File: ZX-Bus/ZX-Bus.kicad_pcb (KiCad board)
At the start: 2 copper layers, 177 x 146 mm, 51 parts, among them J1 DIP-40 Pins, J2 PLS-3, J3 PLS-6, J4 Power, J5 Main board power, J6 12V, J7 5V, J8 Reset, J9 PLS-2R, U1 Z84C00xxP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

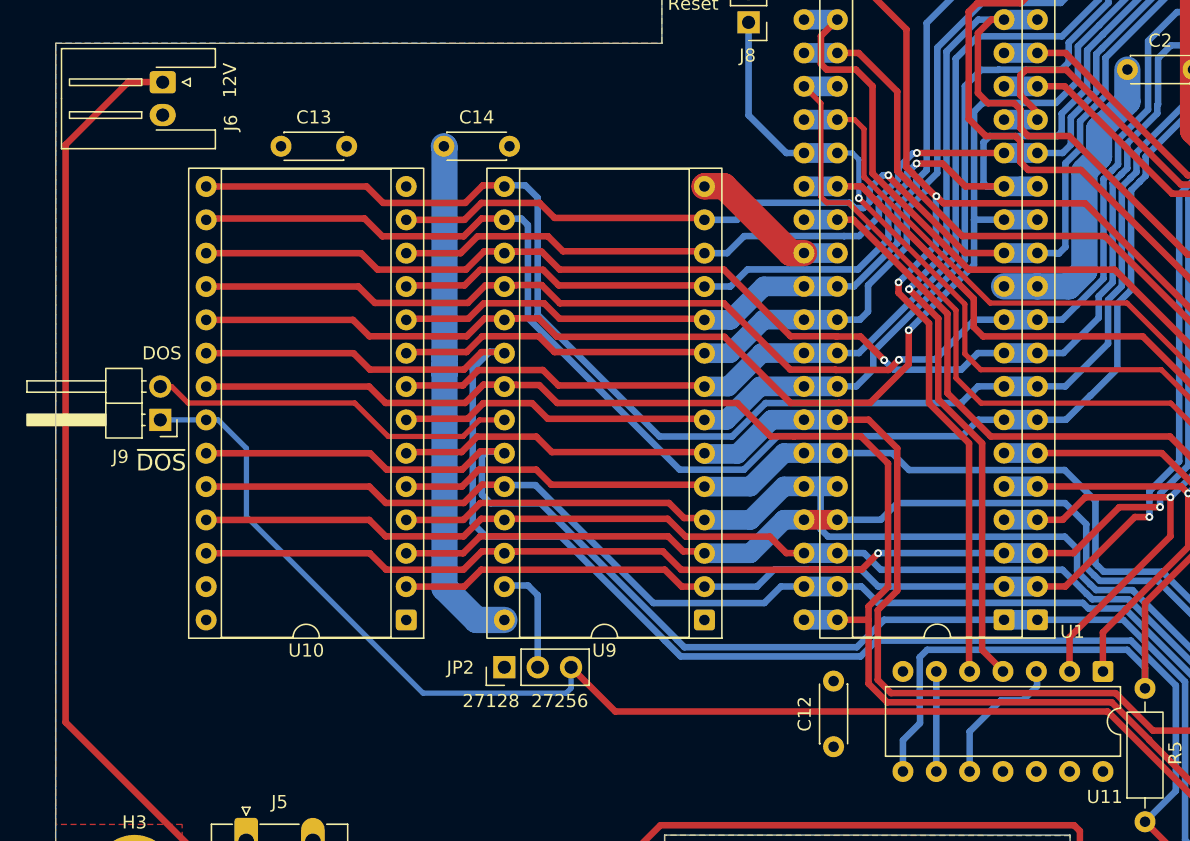
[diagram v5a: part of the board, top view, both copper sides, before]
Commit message: ZX-Bus: Fix ROM type select jumper
We actually need to switch two lines.
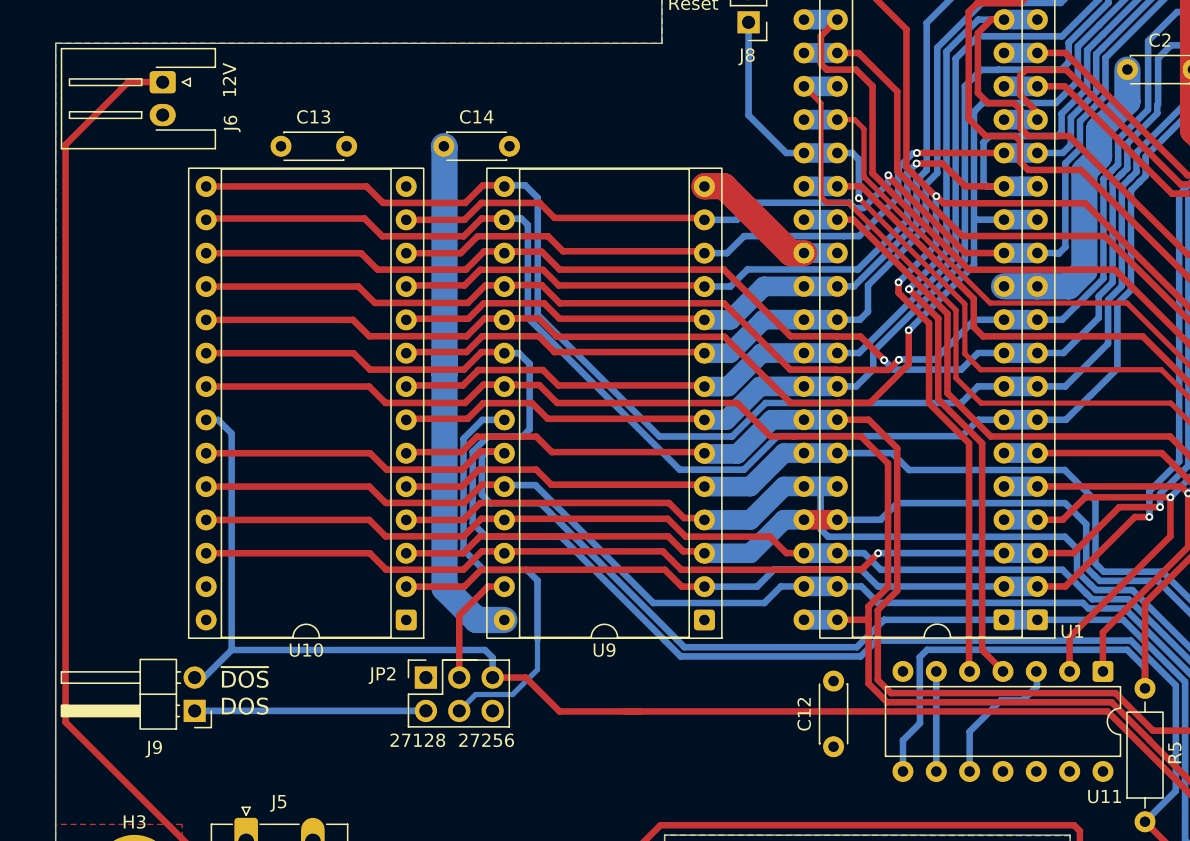
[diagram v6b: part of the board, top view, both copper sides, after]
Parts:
- JP2: footprint Connector_PinHeader_2.54mm:PinHeader_1x03_P2.54mm_Vertical -> Connector_PinHeader_2.54mm:PinHeader_3x09_P2.54mm_Vertical
- moved J9 22.3 mm to (26.4, 182.4)
- moved JP2 6.03 mm to (44.0, 179.8), turned to 0 degrees
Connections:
- J9 pad 1: /~{DOS} -> /DOS
- J9 pad 2: /DOS -> /~{DOS}
- U9 pad 22: /DOS -> Net-(U9-~{OE})
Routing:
- net Net-(U9-~{OE}): track 0.00 -> 32.8 mm
- net /DOS: track 28.3 -> 17.6 mm
- net /~{DOS}: track 258.5 -> 264.8 mm
- net /~{RDR}: track 327.3 -> 330.4 mm
- net Net-(U9-~{PGM}): track 8.33 -> 9.08 mm
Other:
- board text added: "~{DOS} DOS"
- board text removed: "DOS"
- board text removed: "~{DOS}"

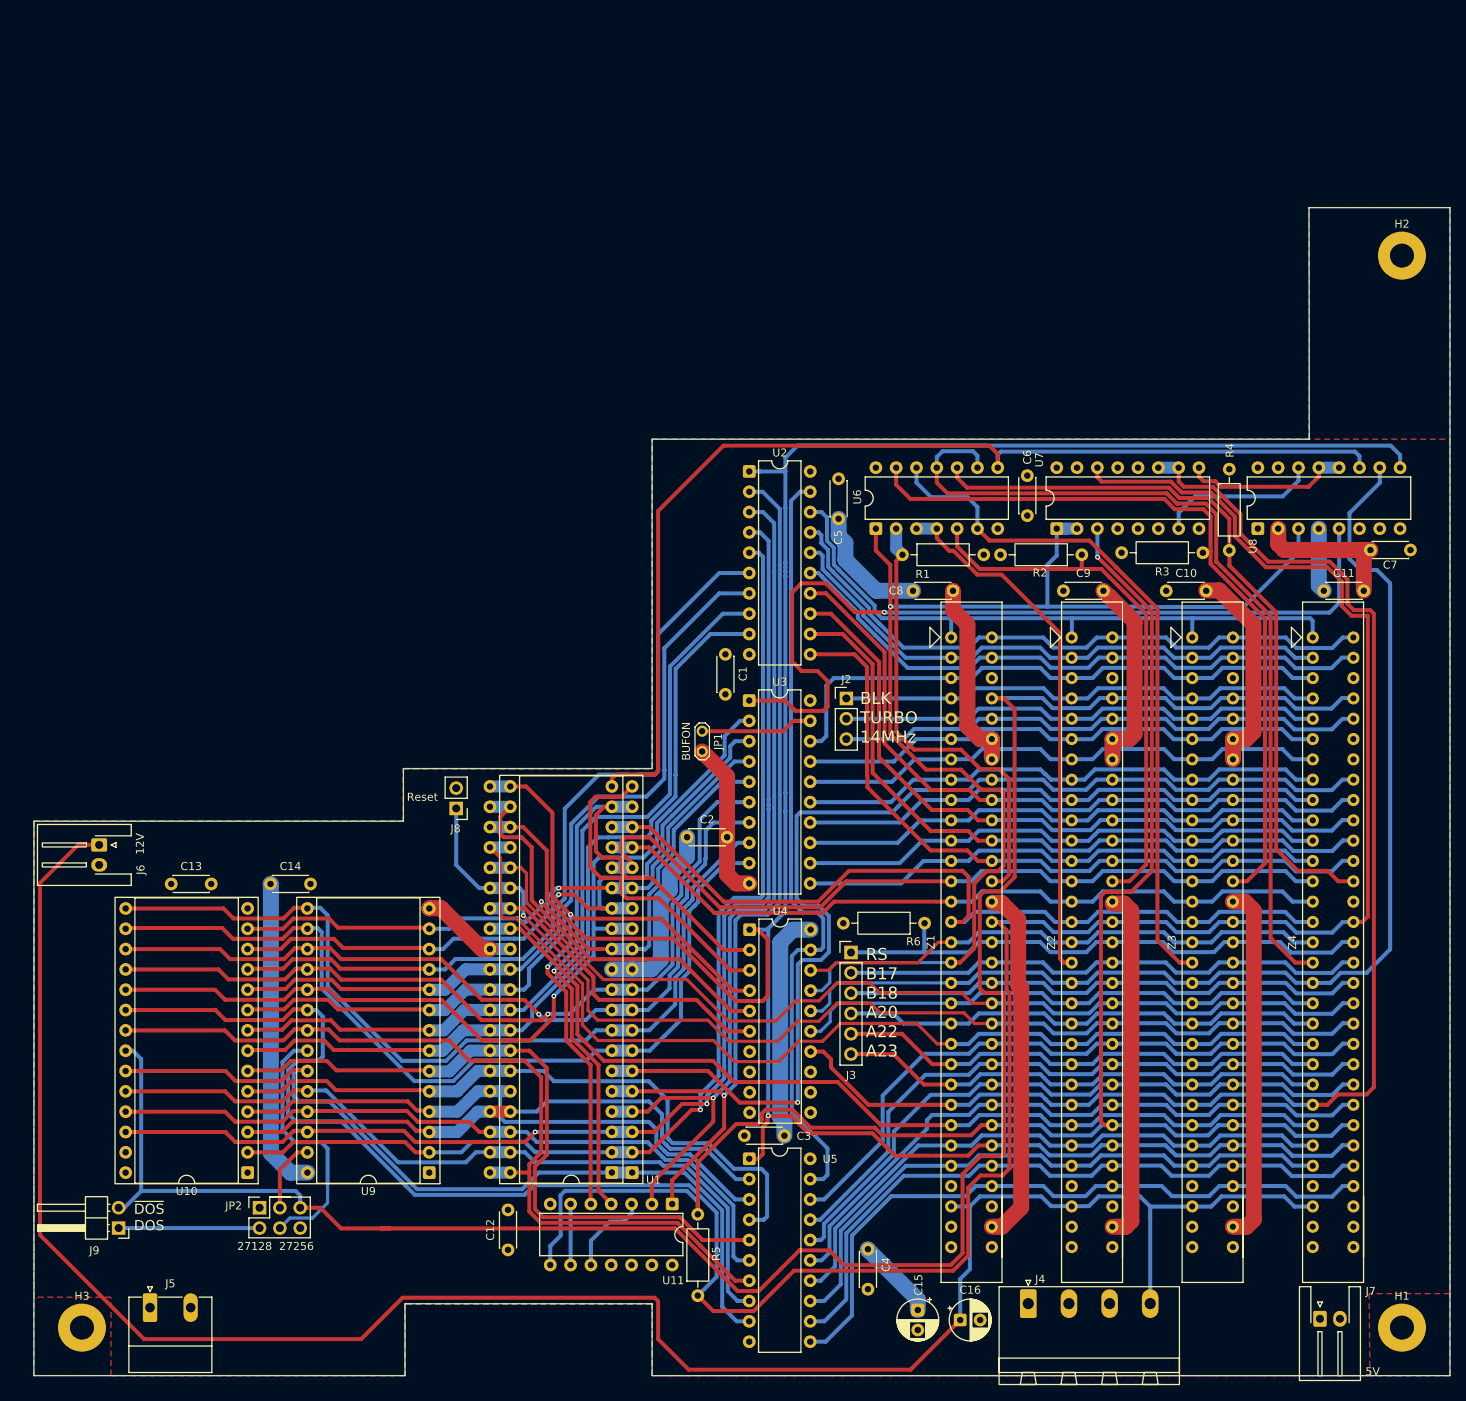
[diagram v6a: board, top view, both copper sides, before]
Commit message: ZX-Bus: More taps
Add 14MHz tap to U2 (on main board). Add some more power headers so that we are
able to connect the board with no need to solder more power cables. It's
possible to drill the main board in those places and install power pins.
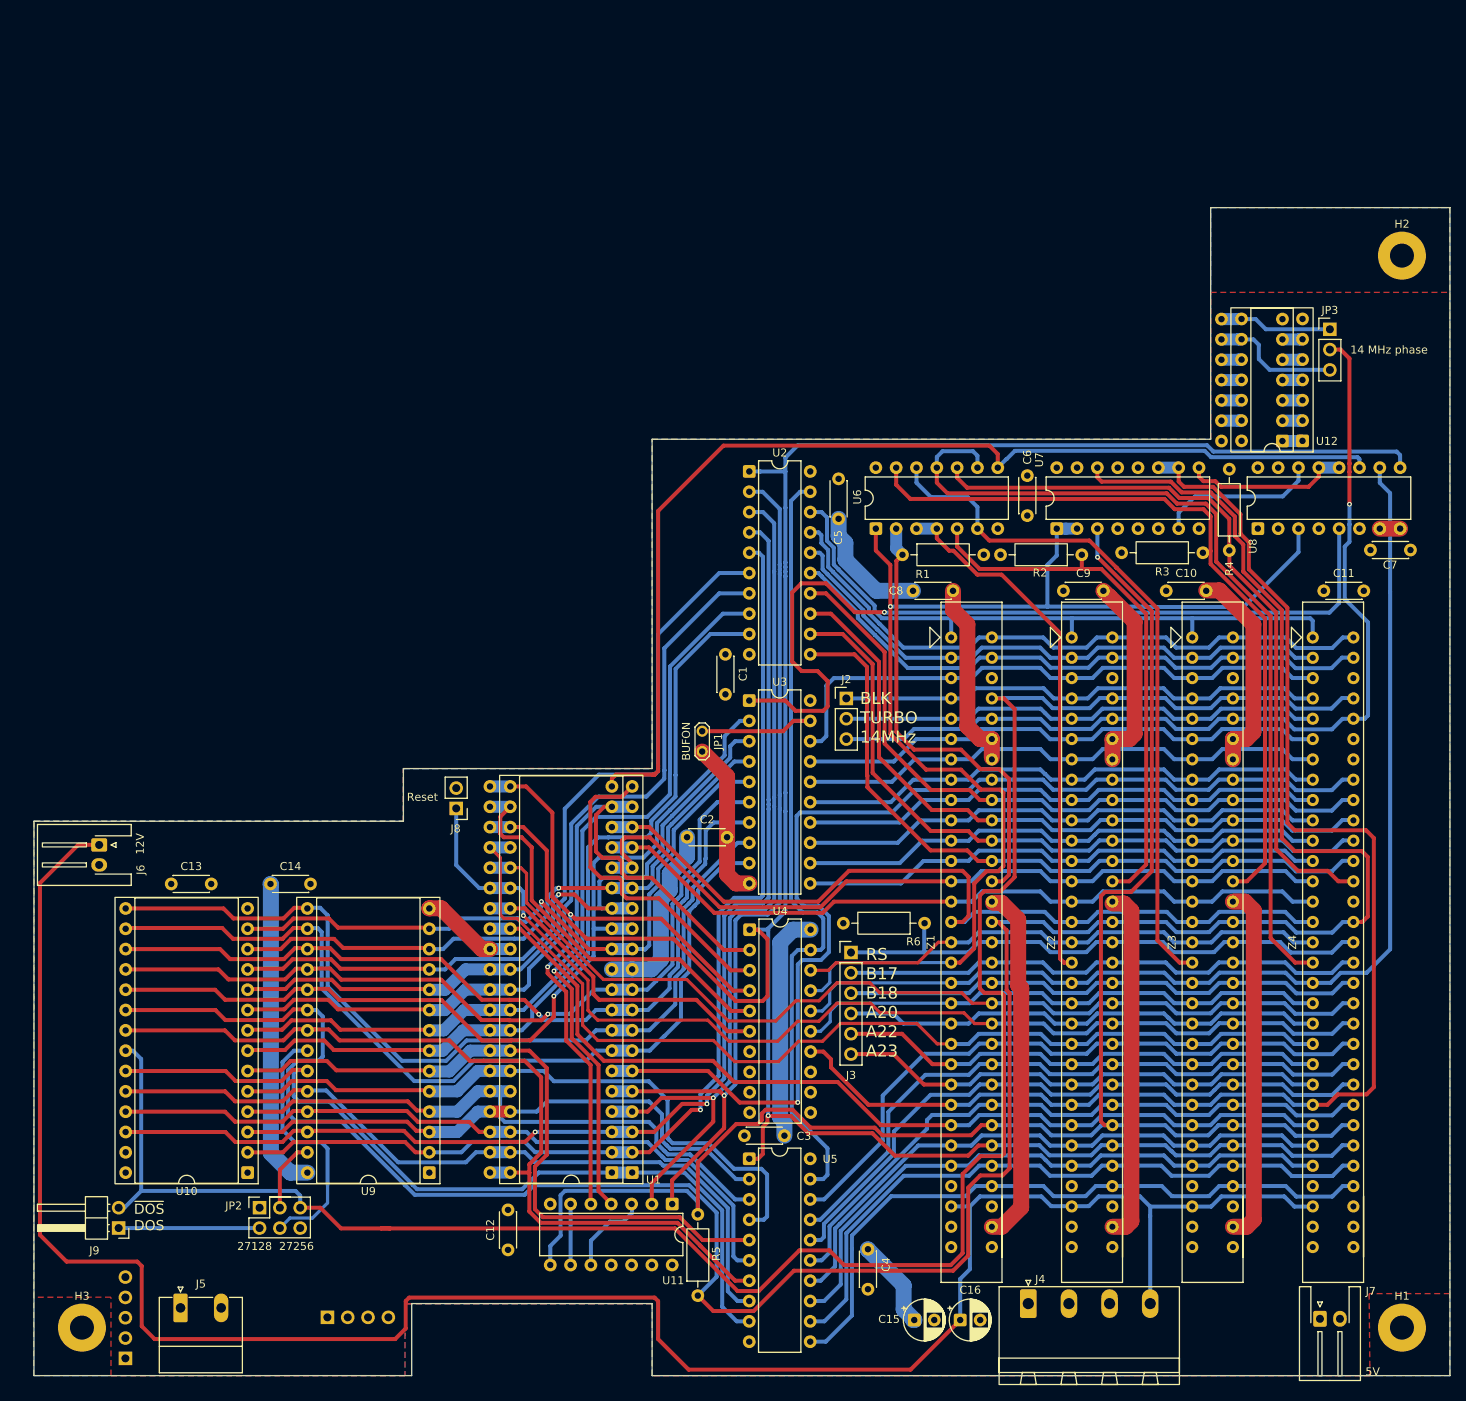
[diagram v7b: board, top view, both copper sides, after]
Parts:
- added J10: DIP14, Package_DIP:DIP-14_W7.62mm-Pins, F.Cu at (171.8, 84.0)
- added J11: PBS-4, Connector_PinSocket_2.54mm:PinSocket_1x04_P2.54mm_Vertical, B.Cu at (52.5, 193.5)
- added J12: PBS-5, Connector_PinSocket_2.54mm:PinSocket_1x05_P2.54mm_Vertical, B.Cu at (27.2, 198.6)
- added JP3: 14 MHz phase, Connector_PinHeader_2.54mm:PinHeader_1x03_P2.54mm_Vertical, F.Cu at (177.8, 70.0)
- added U12: 74LS04, Package_DIP:DIP-14_W7.62mm_Socket, F.Cu at (174.3, 84.0)
- moved J5 3.81 mm to (34.1, 192.3)
- moved C15 1.33 mm to (125.8, 193.9), turned to 0 degrees
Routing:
- net /F: track 67.6 -> 118.6 mm, vias 0 -> 1
- net GND: track 260.1 -> 243.8 mm
- net Net-(J10-Pin_9): track 0.00 -> 16.2 mm
- net Net-(J10-Pin_8): track 0.00 -> 14.1 mm
- net VCC: track 125.1 -> 118.4 mm
- net +12V: track 260.1 -> 266.5 mm
- net /~{RD}: track 145.5 -> 141.2 mm
- net Net-(J10-Pin_6): track 0.00 -> 2.52 mm
- net Net-(J10-Pin_4): track 0.00 -> 2.52 mm
- net Net-(J10-Pin_2): track 0.00 -> 2.52 mm
- net Net-(J10-Pin_5): track 0.00 -> 2.52 mm
- net Net-(J10-Pin_3): track 0.00 -> 2.52 mm
- net Net-(J10-Pin_1): track 0.00 -> 2.52 mm
- net Net-(J10-Pin_13): track 0.00 -> 2.50 mm
- net Net-(J10-Pin_11): track 0.00 -> 2.50 mm
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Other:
- outline, holes or cut-outs redrawn
